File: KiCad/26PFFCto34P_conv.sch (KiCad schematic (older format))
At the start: 9 parts, among them J1 Conn_02x17_Odd_Even, J2 Ready, J3 DSx, J4 2HD, J5 -+, J6 FD_FFC_26p

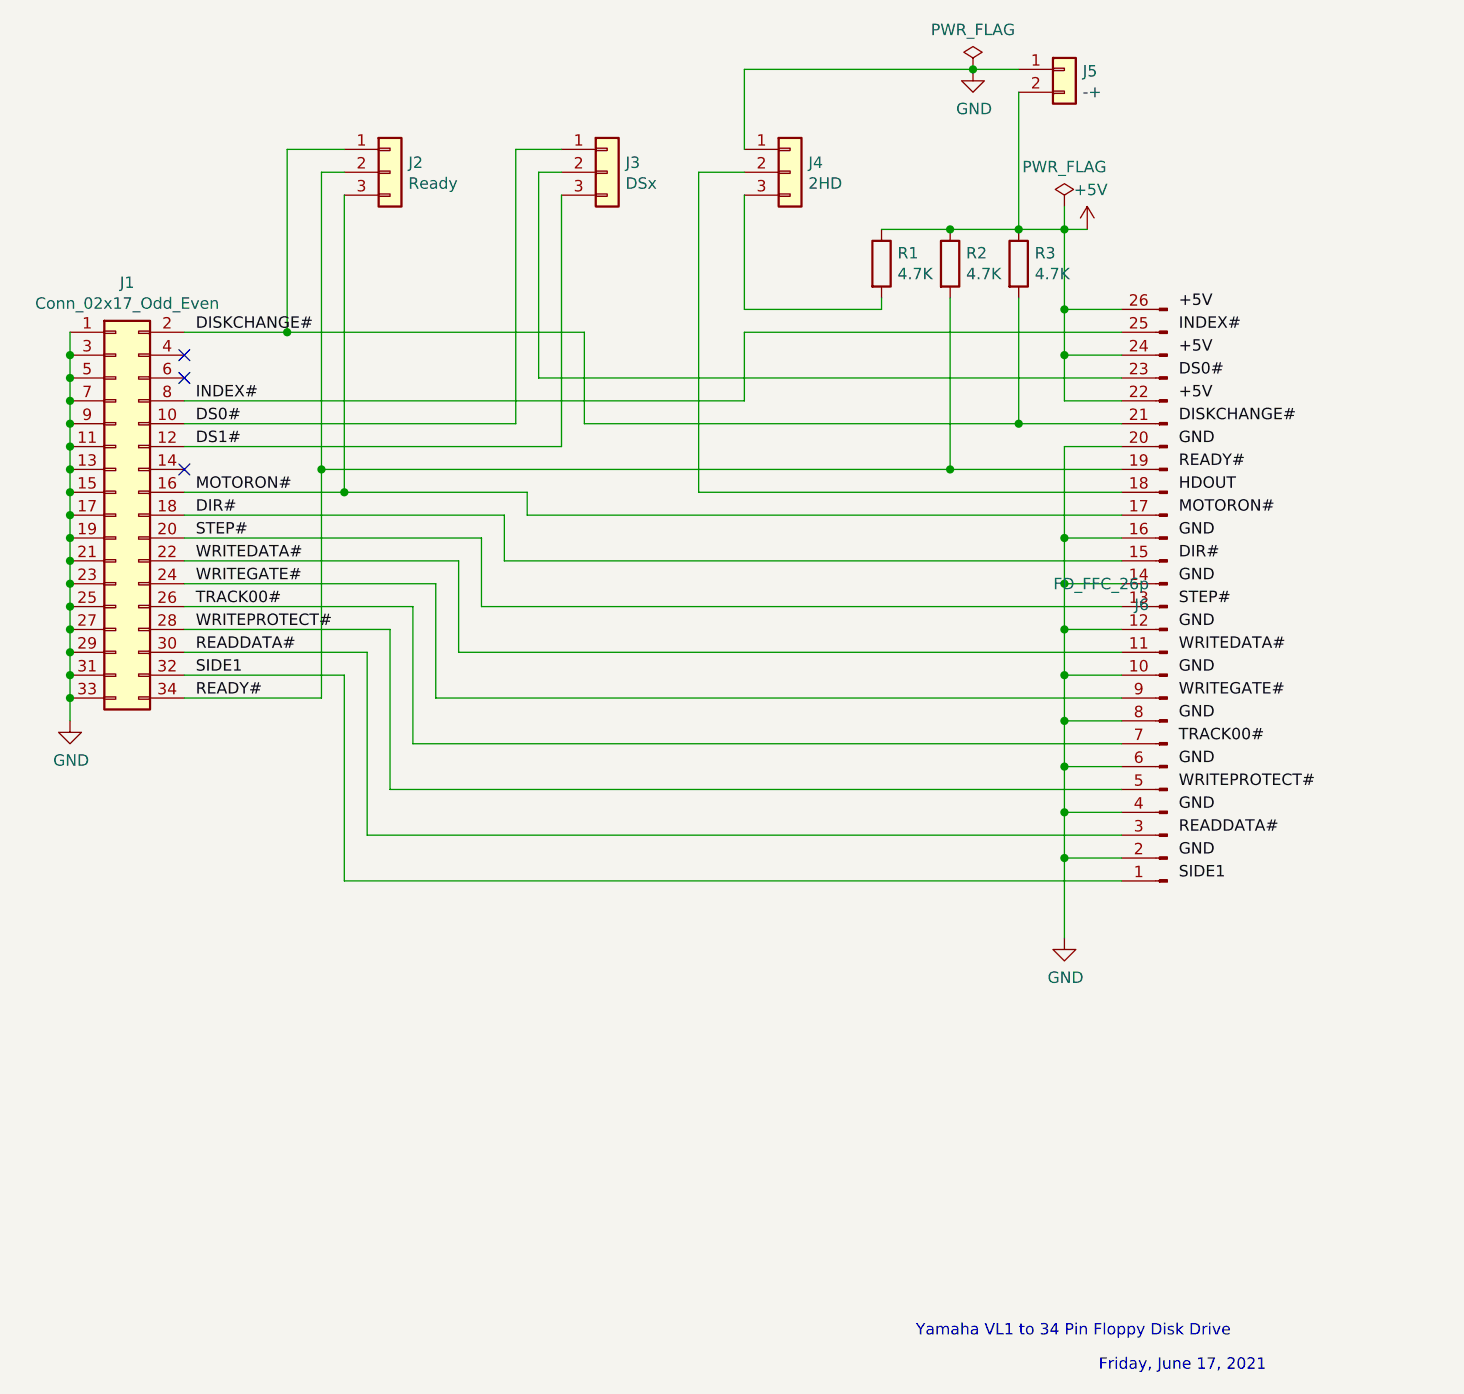
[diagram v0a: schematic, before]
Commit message: DS1 fixed. width 48mm to 50mm
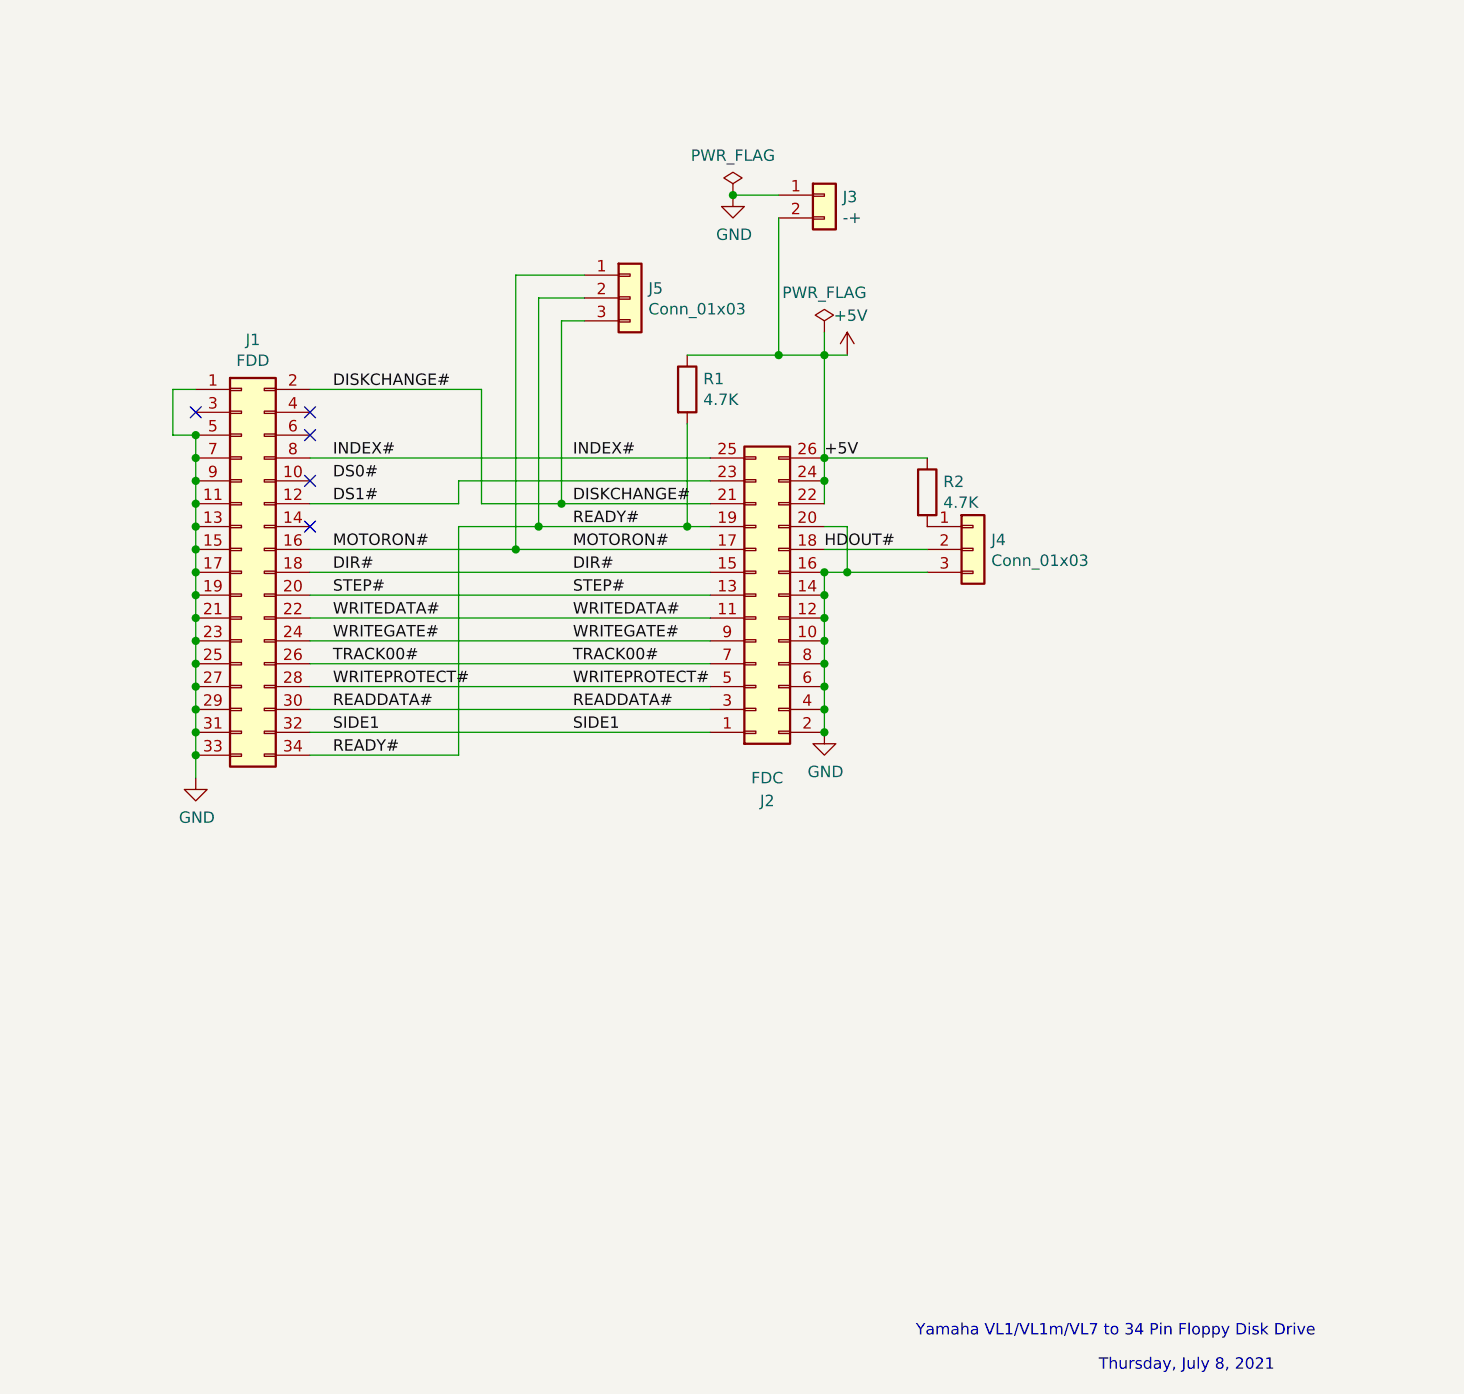
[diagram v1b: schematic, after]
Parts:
- removed J2: Ready, Connector_PinHeader_2.00mm:PinHeader_1x03_P2.00mm_Vertical, symbol Connector_Generic:Conn_01x03
- removed J3: DSx, Connector_PinHeader_2.00mm:PinHeader_1x03_P2.00mm_Vertical, symbol Connector_Generic:Conn_01x03
- removed J6: FD_FFC_26p, kicad_by_BakudaLab:520452645, symbol Connector:Conn_01x26_Male
- removed R3: 4.7K, Resistor_THT:R_Axial_DIN0204_L3.6mm_D1.6mm_P5.08mm_Horizontal, symbol Device:R
- added J2: FDC, kicad_by_BakudaLab:morex520452645, symbol Connector_Generic:Conn_02x13_Odd_Even
- added J5: Conn_01x03, Connector_PinHeader_2.54mm:PinHeader_1x03_P2.54mm_Vertical, symbol Connector_Generic:Conn_01x03
- J1: value Conn_02x17_Odd_Even -> FDD
- J4: value 2HD -> Conn_01x03; footprint Connector_PinHeader_2.00mm:PinHeader_1x03_P2.00mm_Vertical -> Connector_PinHeader_2.54mm:PinHeader_1x03_P2.54mm_Vertical
- renumbered J5 to J3
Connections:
- net +5V: now also J2.22 (Pin_22), J2.24 (Pin_24), J2.26 (Pin_26)
- net DIR#: now also J2.15 (Pin_15)
- net DISKCHANGE#: now also J2.21 (Pin_21), J5.3 (Pin_3)
- net DS0#: no longer J1.10 (Pin_10)
- net DS1#: now also J2.23 (Pin_23)
- net GND: now also J4.3 (Pin_3), J2.10 (Pin_10), J2.12 (Pin_12), J2.14 (Pin_14), J2.16 (Pin_16), J2.2 (Pin_2), J2.20 (Pin_20), J2.4 (Pin_4), J2.6 (Pin_6), J2.8 (Pin_8); no longer J1.3 (Pin_3), J4.1 (Pin_1)
- net INDEX#: now also J2.25 (Pin_25)
- net MOTORON#: now also J2.17 (Pin_17), J5.1 (Pin_1)
- net READDATA#: now also J2.3 (Pin_3)
- net READY#: now also R1.2, J2.19 (Pin_19), J5.2 (Pin_2); no longer R2.2
- net SIDE1: now also J2.1 (Pin_1)
- net STEP#: now also J2.13 (Pin_13)
- net TRACK00#: now also J2.7 (Pin_7)
- net WRITEDATA#: now also J2.11 (Pin_11)
- net WRITEGATE#: now also J2.9 (Pin_9)
- net WRITEPROTECT#: now also J2.5 (Pin_5)
- net HDOUT#: now reaches J4.2 (Pin_2)
- net HDOUT#: now also J2.18 (Pin_18)
- new net: J4.1 (Pin_1), R2.2
- no-connect marks 3 -> 5
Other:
- note added: "Thursday, July 8, 2021"
- note added: "Yamaha VL1/VL1m/VL7 to 34 Pin Floppy Disk Drive"
- note removed: "Friday, June 17, 2021"
- note removed: "Yamaha VL1 to 34 Pin Floppy Disk Drive"
- moved on the sheet: J1, J3

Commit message: Further miniaturization
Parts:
- J2: footprint kicad_by_BakudaLab:morex520452645 -> 26PFFCto34P_conv:morex520452645
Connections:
- net DIR# renamed DIR
- net DISKCHANGE# renamed DISKCHANGE
- net DS1# renamed DRIVESELECT
- net INDEX# renamed INDEX
- net READDATA# renamed READDATA
- net READY# renamed READY
- net STEP# renamed STEP
- net TRACK00# renamed TRACK00
- net WRITEDATA# renamed WRITEDATA
- net WRITEGATE# renamed WRITEGATE
- net WRITEPROTECT# renamed WRITEPROTECT
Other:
- note added: "26P FFC to 34P Shugart Connector"
- note removed: "Yamaha VL1/VL1m/VL7 to 34 Pin Floppy Disk Drive"
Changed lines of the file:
@@
 $EndComp
 Text Label 4850 4950 0    50   ~ 0
-READY#
+READY#DISKCHANGE#
 Text Label 4850 4850 0    50   ~ 0
-SIDE1
+SIDE1SELECT#
 Text Label 4850 4750 0    50   ~ 0
 READDATA#
@@
 	4750 4950 5400 4950
 Text Notes 7400 7500 0    50   ~ 0
-Yamaha VL1/VL1m/VL7 to 34 Pin Floppy Disk Drive
+26P FFC to 34P Shugart Connector
 Text Notes 8200 7650 0    50   ~ 0
 Thursday, July 8, 2021
@@
 U 1 1 60DE024B
 P 6700 4250
-F 0 "J2" H 6750 5150 50  0000 C CNN
-F 1 "FDC" H 6750 5050 50  0000 C CNN
-F 2 "kicad_by_BakudaLab:morex520452645" H 6700 4250 50  0001 C CNN
+F 0 "J2" H 6750 3400 50  0000 C CNN
+F 1 "FDC" H 6750 3500 50  0000 C CNN
+F 2 "26PFFCto34P_conv:morex520452645" H 6700 4250 50  0001 C CNN
 F 3 "~" H 6700 4250 50  0001 C CNN
 	1    6700 4250
@@
 $EndComp
 Text Label 5900 3650 0    50   ~ 0
-INDEX#
+INDEX
 Text Label 5900 3850 0    50   ~ 0
-DISKCHANGE#
-Text Label 5900 4050 0    50   ~ 0
-MOTORON#
+DISKCHANGE
 Text Label 5900 4150 0    50   ~ 0
-DIR#
+DIR
 Text Label 5900 4250 0    50   ~ 0
-STEP#
+STEP
 Text Label 5900 4350 0    50   ~ 0
-WRITEDATA#
+WRITEDATA
 Text Label 5900 4450 0    50   ~ 0
-WRITEGATE#
+WRITEGATE
 Text Label 5900 4550 0    50   ~ 0
-TRACK00#
+TRACK00
 Text Label 5900 4650 0    50   ~ 0
-WRITEPROTECT#
+WRITEPROTECT
 Text Label 5900 4750 0    50   ~ 0
-READDATA#
+READDATA
 Text Label 5900 4850 0    50   ~ 0
 SIDE1
@@
 Connection ~ 4250 3550
 Text Label 4850 3350 0    50   ~ 0
-DISKCHANGE#
+MODESELECT#
 NoConn ~ 4750 3750
 Wire Wire Line
@@
 	7000 3750 7000 3650
 Text Label 5900 3950 0    50   ~ 0
-READY#
+READY
 $Comp
 L Device:R R1
@@
 	6800 3200 6400 3200
 Connection ~ 6800 3200
-Wire Wire Line
-	6400 3500 6400 3950
-Connection ~ 6400 3950
-Wire Wire Line
-	6400 3950 6500 3950
 $Comp
 L Connector_Generic:Conn_01x03 J5
@@
 $EndComp
 Wire Wire Line
-	6500 3850 5850 3850
-Wire Wire Line
 	5850 3850 5850 3050
 Wire Wire Line
@@
 Connection ~ 5750 3950
 Wire Wire Line
+	5650 2850 5950 2850
+Wire Wire Line
+	4750 3350 5500 3350
+Wire Wire Line
+	5500 3350 5500 3850
+Connection ~ 5850 3850
+Wire Wire Line
 	5750 3950 6400 3950
-Wire Wire Line
-	5650 4050 5650 2850
-Wire Wire Line
-	5650 2850 5950 2850
+Text Label 5900 3750 0    50   ~ 0
+DRIVESELECT
+Wire Wire Line
+	5850 3850 6500 3850
+Wire Wire Line
+	6400 3500 6400 3950
+Connection ~ 6400 3950
+Wire Wire Line
+	6400 3950 6500 3950
+Wire Wire Line
+	5650 2850 5650 4050
+Wire Wire Line
+	5500 3850 5850 3850
+Wire Wire Line
+	6500 4050 5650 4050
 Connection ~ 5650 4050
-Wire Wire Line
-	5650 4050 6500 4050
-Wire Wire Line
-	4750 3350 5500 3350
-Wire Wire Line
-	5500 3350 5500 3850
-Wire Wire Line
-	5500 3850 5850 3850
-Connection ~ 5850 3850
 $EndSCHEMATC
